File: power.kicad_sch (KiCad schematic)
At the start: 30 parts, among them U10 TLV75533PDBVR, U6 LMR51420YDDCR, U7 LMR51420YDDCR, U9 TLV75533PDBVR

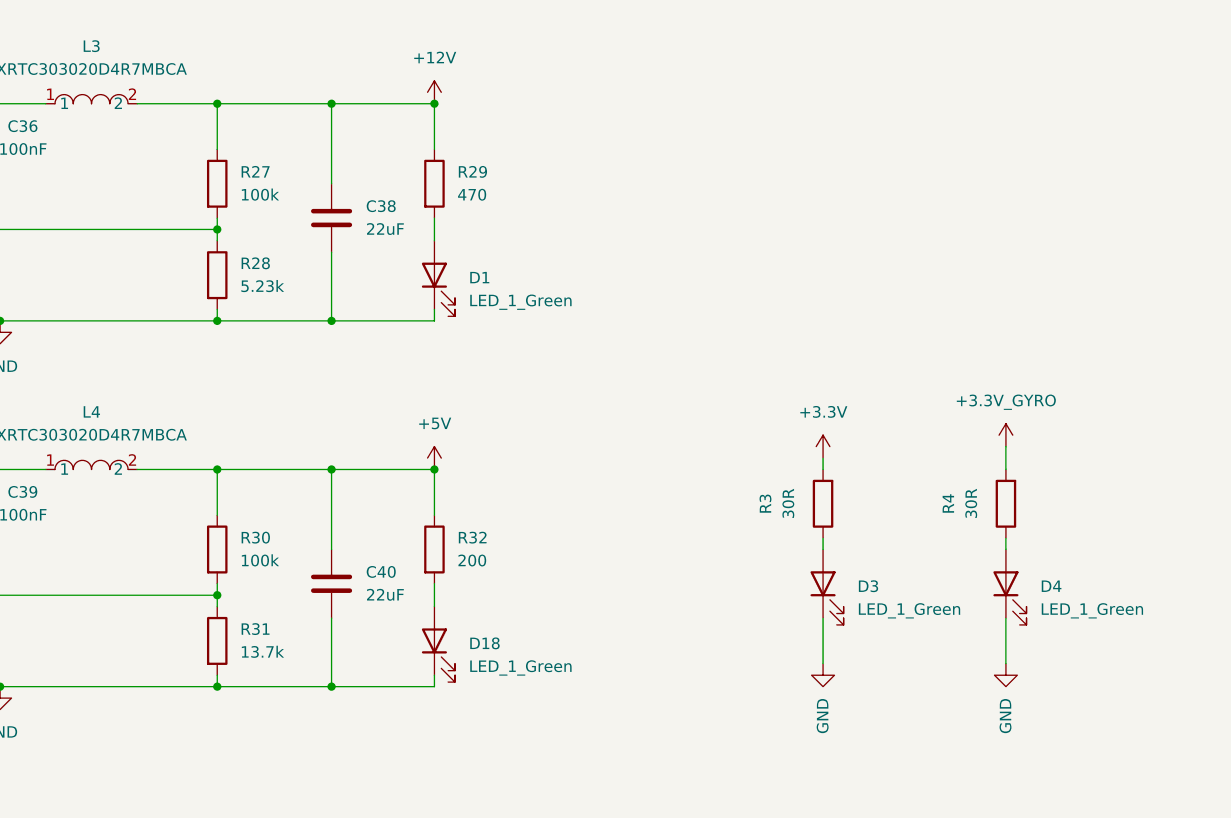
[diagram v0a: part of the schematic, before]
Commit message: almost finished routing
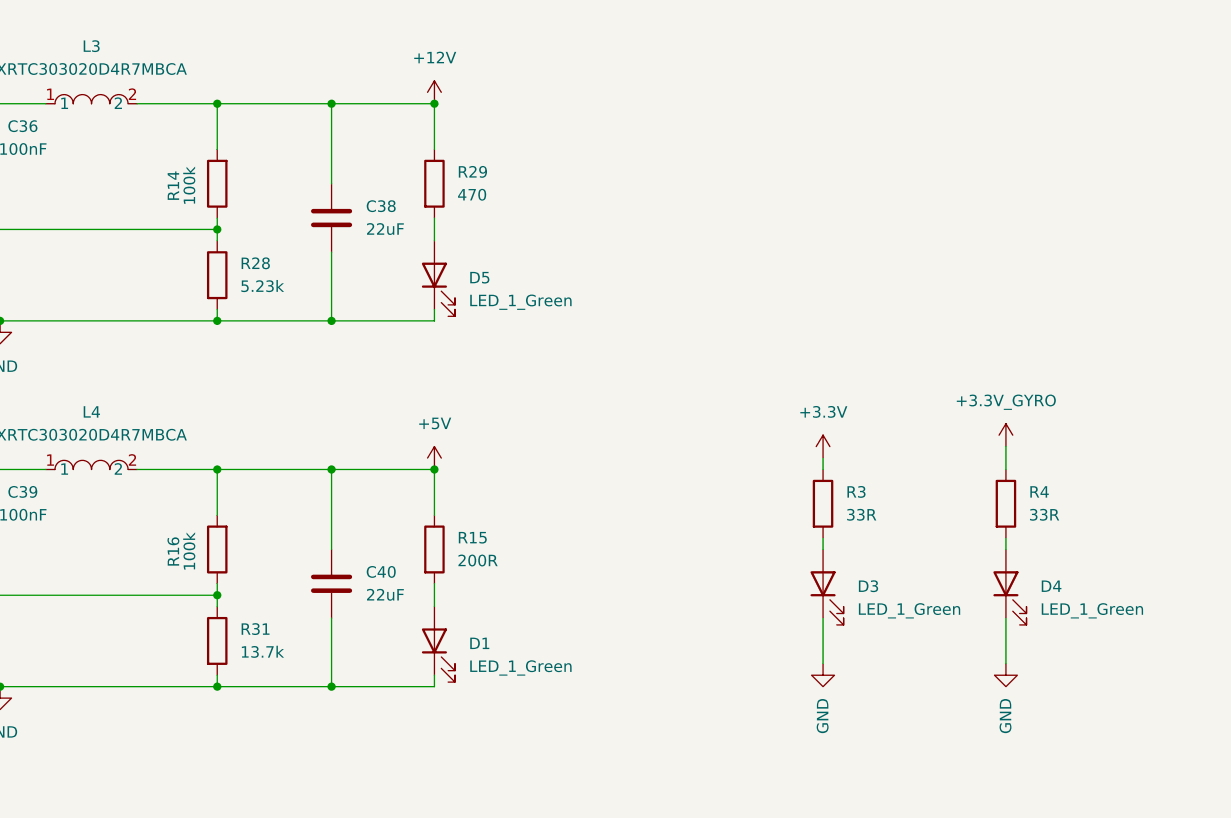
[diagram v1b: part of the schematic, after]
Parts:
- removed D18: LED_1_Green, LED_SMD:LED_0603_1608Metric, symbol Device:LED
- removed R27, R30: 100k, Resistor_SMD:R_0402_1005Metric, symbol Device:R
- removed R32: 200, Resistor_SMD:R_0402_1005Metric, symbol Device:R
- added D5: LED_1_Green, LED_SMD:LED_0603_1608Metric, symbol Device:LED
- added R14, R16: 100k, Resistor_SMD:R_0402_1005Metric, symbol Device:R
- added R15: 200R, Resistor_SMD:R_0402_1005Metric, symbol Device:R
- D1, D3, D4: LCSC (none) -> C2994781
- R28: LCSC (none) -> C2684530
- R29, R31: LCSC (none) -> C114877
- R3, R4: value 30R -> 33R; LCSC (none) -> C25105
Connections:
- net +12V: now also R14.2
- net +3.3V: now also R3.1; no longer R3.2
- net +3.3V_GYRO: now also R4.1; no longer R4.2
- net +5V: now also R15.1, R16.2
- net GND: now also D5.1 (K)
- net at D4.2 (A): now also R4.2; no longer R4.1
- net at R28.1, U6.4 (FB): now also R14.1
- net at D3.2 (A): now also R3.2; no longer R3.1
- net at R29.2: now also D5.2 (A); no longer D1.2 (A)
- net at R31.1, U7.4 (FB): now also R16.1
- new net: D1.2 (A), R15.2

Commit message: Final routing
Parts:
- R31: LCSC C114877 -> C2933072
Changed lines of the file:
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@@
 			)
 		)
-		(property "LCSC" "C114877"
+		(property "LCSC" "C2933072"
 			(at 152.4 92.71 0)
 			(effects

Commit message: Switched to RP2354A and re-routed
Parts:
- removed C16: 4.7uF 50v, Capacitor_SMD:C_0805_2012Metric, symbol Device:C
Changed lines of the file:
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@@
 	(paper "A4")
-	(junction
-		(at 77.47 57.15)
-		(diameter 0)
-		(color 0 0 0 0)
-	)
 	(junction
 		(at 152.4 33.02)
@@
 	(wire
 		(pts
-			(xy 68.58 41.91) (xy 68.58 33.02)
-		)
-		(stroke
-			(width 0)
-			(type default)
-		)
-	)
-	(wire
-		(pts
 			(xy 260.35 128.27) (xy 260.35 129.54)
 		)
@@
 	(wire
 		(pts
-			(xy 68.58 33.02) (xy 77.47 33.02)
-		)
-		(stroke
-			(width 0)
-			(type default)
-		)
-	)
-	(wire
-		(pts
 			(xy 77.47 57.15) (xy 77.47 49.53)
 		)
@@
 	(wire
 		(pts
-			(xy 68.58 57.15) (xy 77.47 57.15)
-		)
-		(stroke
-			(width 0)
-			(type default)
-		)
-	)
-	(wire
-		(pts
 			(xy 114.3 78.74) (xy 114.3 81.28)
 		)
@@
 		(pts
 			(xy 124.46 33.02) (xy 133.35 33.02)
-		)
-		(stroke
-			(width 0)
-			(type default)
-		)
-	)
-	(wire
-		(pts
-			(xy 68.58 49.53) (xy 68.58 57.15)
 		)
 		(stroke
@@
 					(unit 1)
 				)
-			)
-		)
-	)
-	(symbol
-		(lib_id "Device:C")
-		(at 68.58 45.72 0)
-		(unit 1)
-		(exclude_from_sim no)
-		(in_bom yes)
-		(on_board yes)
-		(dnp no)
-		(fields_autoplaced yes)
-		(property "Reference" "C16"
-			(at 72.39 44.4499 0)
-			(effects
-				(font
-					(size 1.27 1.27)
-				)
-				(justify left)
-			)
-		)
-		(property "Value" "4.7uF 50v"
-			(at 72.39 46.9899 0)
-			(effects
-				(font
-					(size 1.27 1.27)
-				)
-				(justify left)
-			)
-		)
-		(property "Footprint" "Capacitor_SMD:C_0805_2012Metric"
-			(at 69.5452 49.53 0)
-			(effects
-				(font
-					(size 1.27 1.27)
-				)
-				(hide yes)
-			)
-		)
-		(property "Datasheet" "~"
-			(at 68.58 45.72 0)
-			(effects
-				(font
-					(size 1.27 1.27)
-				)
-				(hide yes)
-			)
-		)
-		(property "Description" "Unpolarized capacitor"
-			(at 68.58 45.72 0)
-			(effects
-				(font
-					(size 1.27 1.27)
-				)
-				(hide yes)
-			)
-		)
-		(property "LCSC" "C98192"
-			(at 68.58 45.72 0)
-			(effects
-				(font
-					(size 1.27 1.27)
-				)
-				(hide yes)
-			)
-		)
-		(pin "1"
-		)
-		(pin "2"
-		)
-		(instances
-			(project "OpenFC"
-				(path "/fb88b6f9-ee39-4640-a9d4-04a17ceeac64/f8522f96-c979-41d2-ae00-e5ad899a3161"
-					(reference "C16")
-					(unit 1)
-				)

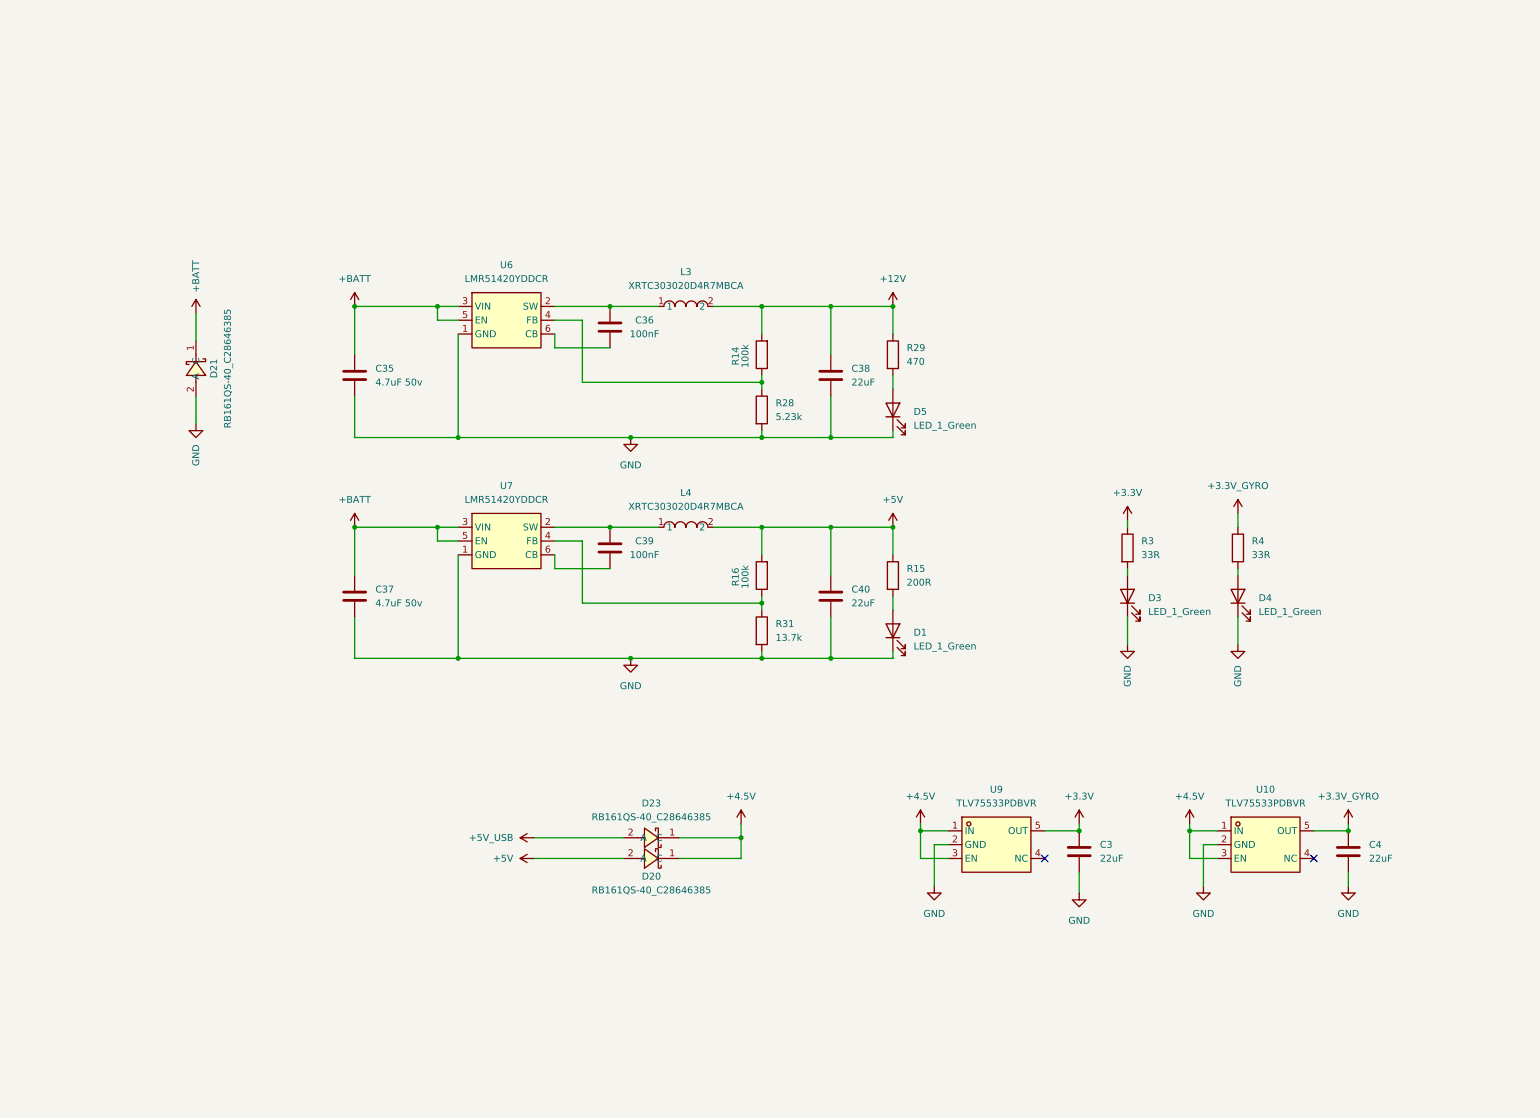
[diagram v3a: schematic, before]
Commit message: Added Open-OSD-X and new layout
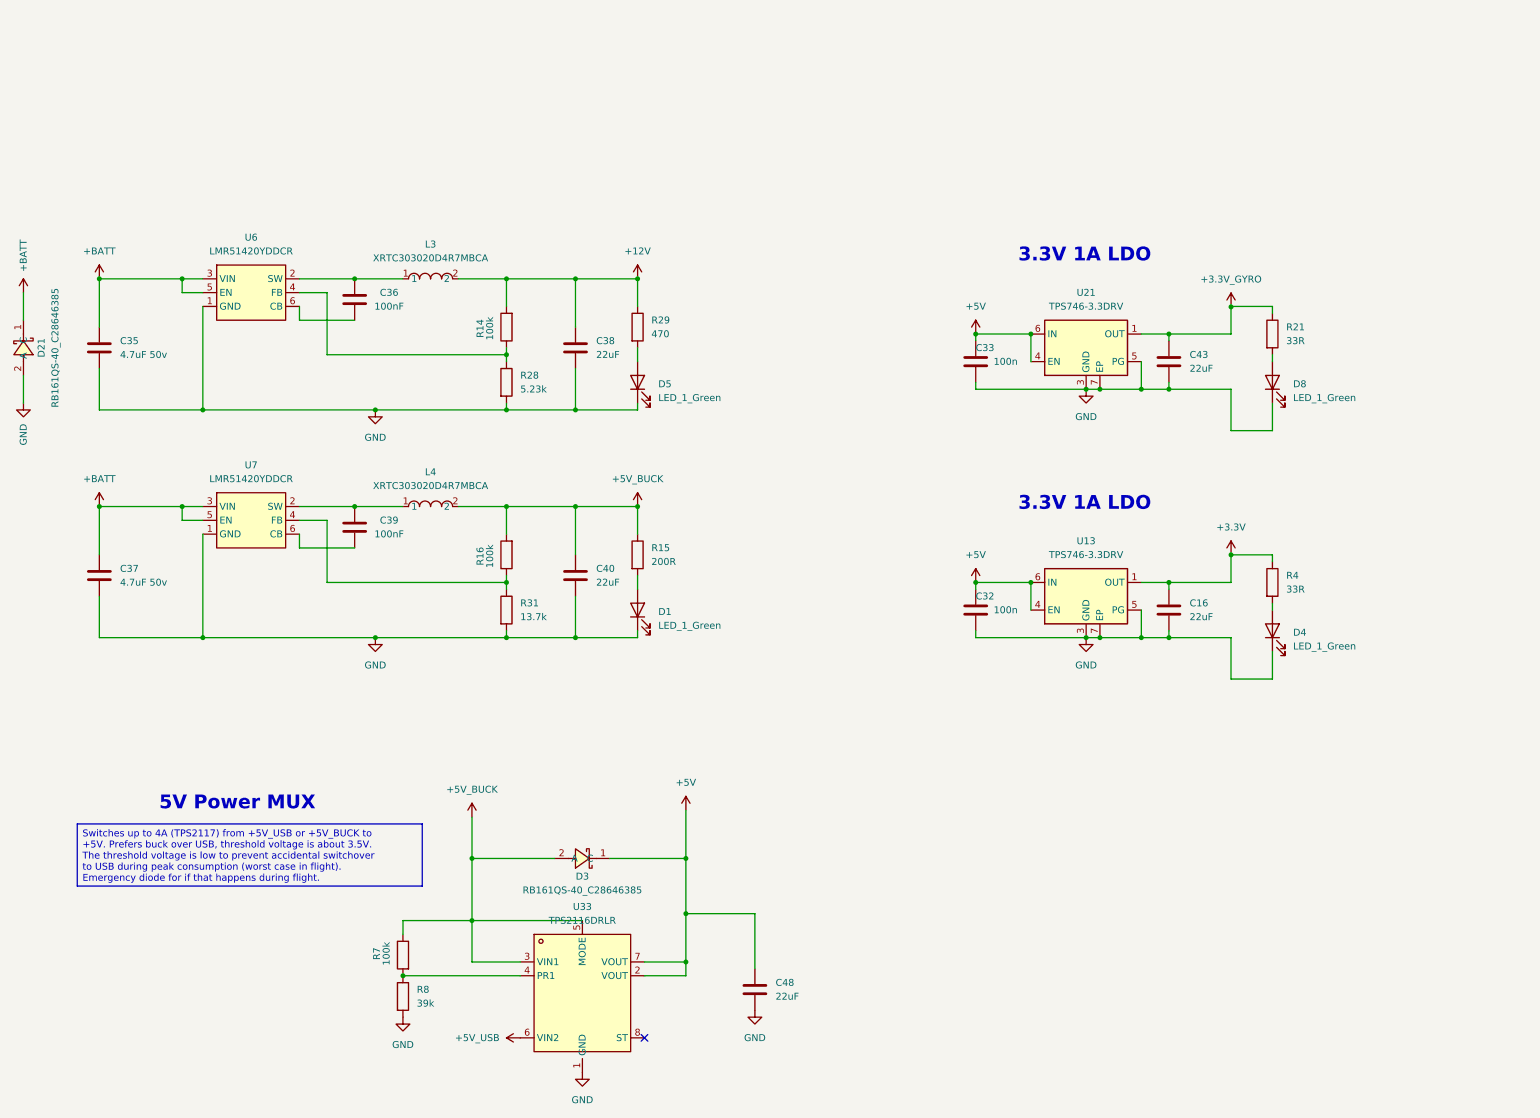
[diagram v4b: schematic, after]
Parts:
- removed C3, C4: 22uF, Capacitor_SMD:C_0402_1005Metric, symbol Device:C
- removed D20, D23: RB161QS-40_C28646385, lib:SOD-882_L1.0-W0.6-RD, symbol lib:RB161QS-40_C28646385
- removed D3: LED_1_Green, LED_SMD:LED_0603_1608Metric, symbol Device:LED
- removed R3: 33R, Resistor_SMD:R_0402_1005Metric, symbol Device:R
- removed U10, U9: TLV75533PDBVR, lib:SOT-23-5_L3.0-W1.7-P0.95-LS2.8-BR, symbol lib:TLV75533PDBVR
- added C16, C43: 22uF, Capacitor_SMD:C_0402_1005Metric, symbol Device:C
- added C32, C33: 100n, Capacitor_SMD:C_0402_1005Metric, symbol Device:C
- added C48: 22uF, Capacitor_SMD:C_0603_1608Metric, symbol Device:C
- added D3: RB161QS-40_C28646385, lib:SOD-882_L1.0-W0.6-RD, symbol lib:RB161QS-40_C28646385
- added D8: LED_1_Green, LED_SMD:LED_0603_1608Metric, symbol Device:LED
- added R21: 33R, Resistor_SMD:R_0402_1005Metric, symbol Device:R
- added R7: 100k, Resistor_SMD:R_0402_1005Metric, symbol Device:R
- added R8: 39k, Resistor_SMD:R_0402_1005Metric, symbol Device:R
- added U13, U21: TPS746-3.3DRV, Package_SON:WSON-6-1EP_2x2mm_P0.65mm_EP1x1.6mm, symbol Regulator_Linear:LP5912-3.3DRV
- added U33: TPS2116DRLR, lib:SOT-583-8_L2.1-W1.6-P0.50-LS1.6-BL, symbol lib:TPS2116DRLR
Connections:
- net +3.3V: now also R4.1, C16.1, U13.1 (OUT)
- net +3.3V_GYRO: now also C43.1, R21.1, U21.1 (OUT); no longer R4.1
- net +5V: now also C32.1, C33.1, C48.1, D3.1 (C), U13.4 (EN), U13.6 (IN), U21.4 (EN), U21.6 (IN), U33.2 (VOUT), U33.7 (VOUT); no longer C40.1, L4.2, R15.1, R16.2
- net +5V_USB: now also U33.6 (VIN2)
- net GND: now also C16.2, C32.2, C33.2, C43.2, C48.2, D8.1 (K), R8.2, U13.3 (GND), U13.5 (PG), U13.7 (EP), U21.3 (GND), U21.5 (PG), U21.7 (EP), U33.1 (GND)
- new net: D8.2 (A), R21.2
- new net: R7.2, R8.1, U33.4 (PR1)
- new net +5V_BUCK: C40.1, D3.2 (A), L4.2, R15.1, R16.2, R7.1, U33.3 (VIN1), U33.5 (MODE)
- no-connect marks 2 -> 1
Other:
- note added: "3.3V 1A LDO"
- note added: "5V Power MUX"
- moved on the sheet: C35, C36, C37, C38, C39, C40, D1, D21, D4, D5, L3, L4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

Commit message: Ordered first revision
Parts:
- removed D8: LED_1_Green, LED_SMD:LED_0603_1608Metric, symbol Device:LED
- removed R21: 33R, Resistor_SMD:R_0402_1005Metric, symbol Device:R
- removed U21: TPS746-3.3DRV, Package_SON:WSON-6-1EP_2x2mm_P0.65mm_EP1x1.6mm, symbol Regulator_Linear:LP5912-3.3DRV
- added D7: LED_1_Green, LED_SMD:LED_0603_1608Metric, symbol Device:LED
- added Q1: DMN1150UFB-7B, lib:DFN-3L_L1.0-W0.6-P0.65-BR, symbol lib:DMN1150UFB-7B
- added R12: 200R, Resistor_SMD:R_0402_1005Metric, symbol Device:R
- added U11: LP5900SDX-1.8/NOPB, lib:WSON-6_L2.5-W2.2-P0.65-BL-EP, symbol lib:LP5900SDX-1.8_NOPB
- added U21: NCV8187AMT180TAG, lib:WDFN-6_L2.0-W2.0-P0.65-BL-EP, symbol lib:NCV8187AMT180TAG
- C43: value 22uF -> 470nF
- R4: value 33R -> 30R; LCSC C25105 -> C138007
- U13: LCSC (none) -> C2868202
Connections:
- net +5V: now also R12.1, U11.4 (EN), U11.6 (IN)
- net GND: now also Q1.2 (S), U11.3 (GND), U11.7 (EP)
- net +3.3V_GYRO renamed +1.8V_GYRO
- net +1.8V_GYRO: now also Q1.1 (G), U11.1 (OUT)
- new net: D7.1 (K), Q1.3 (D)
- new net: D7.2 (A), R12.2
- no-connect marks 1 -> 3
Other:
- note added: "1.8V 150mA LDO (high PSRR)"
- note added: "even Better PSRR:"
- moved on the sheet: C33, C43
